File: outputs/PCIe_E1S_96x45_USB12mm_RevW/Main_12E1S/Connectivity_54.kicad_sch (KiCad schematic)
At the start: 12 parts, among them U512 SN74AXC1T45DCKR / HPDA 3.3V t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, U601 9ZXL0851EKILFT / CPU common c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, U602 9ZXL0851EKILFT / CPU common c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, U603 9FGV0241AKLF / DNP ALTERNATE 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, U604 9DML0451AKILF / DNP ALTERNATE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, U605 TPS3808G09DBVR / SUPPORT NETW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, U606 W25Q32JWSSIQ_C2980995 / SUPPO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, U607 TCA9548ARGER / SUPPORT NETWOR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, U701 W25Q256JWPIQ / 1.8V 32MiB BIOS, U702 TPS7A0215PDBVR / RTC 1.5V, U901 TPS548D22RVFR / 0.9004V 40A r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, U902 TPSM63610RDFR / 1.8V 8A

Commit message: Reaudit retained E1S source and improve local converter current paths
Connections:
- net /CPU_PERST_1V8_N renamed /TBT_PCIE_PERST_3V3_N
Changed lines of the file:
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@@
 (kicad_sch (version 20250114) (generator "eeschema") (paper "A2") (title_block (title "Main_12E1S / Connectivity 54") (date "2026-10-17") (rev "W") (comment 1 "FICTIONAL reordered PEX90064 map; CPU288V 32GB MoP; layout and routing study only"))
-(symbol (lib_id "Local:PART_U512") (at 74.93 73.66 0) (unit 1) (in_bom yes) (on_board yes) (dnp no) (property "Reference" "U512" (at 74.93 64.85 0) (effects (font (size 1 1))))(property "Value" "SN74AXC1T45DCKR / HPDA 3.3V to 1.8V" (at 74.93 61.849999999999994 0) (effects (font (size 1 1))))(property "Footprint" "Local:SOT-363_SC-70-6" (at 74.93 73.66 0) (effects (font (size 1 1)) (hide yes)))(pin "1")(pin "2")(pin "3")(pin "4")(pin "5")(pin "6")(instances (project "Main_12E1S" (path "/c33a6c5d-1a9e-4453-a37d-d3058a6ae0e3/4713fd16-f2bf-49a2-84a4-e44d648d003c" (reference "U512") (unit 1)))))
+(symbol (lib_id "Local:PART_U512") (at 74.93 73.66 0) (unit 1) (in_bom yes) (on_board yes) (dnp no) (property "Datasheet" "https://www.ti.com/lit/ds/symlink/sn74axc1t45.pdf" (at 0 0 0) (effects (font (size 1 1)) (hide yes)))(property "Reference" "U512" (at 74.93 64.85 0) (effects (font (size 1 1))))(property "Value" "SN74AXC1T45DCKR / HPDA 3.3V to 1.8V" (at 74.93 61.849999999999994 0) (effects (font (size 1 1))))(property "Footprint" "Local:SOT-363_SC-70-6" (at 74.93 73.66 0) (effects (font (size 1 1)) (hide yes)))(pin "1")(pin "2")(pin "3")(pin "4")(pin "5")(pin "6")(instances (project "Main_12E1S" (path "/c33a6c5d-1a9e-4453-a37d-d3058a6ae0e3/4713fd16-f2bf-49a2-84a4-e44d648d003c" (reference "U512") (unit 1)))))
 (global_label "/CPU_VCCPRIM_1P8" (shape passive) (at 59.690000000000005 71.11999999999999 180) (effects (font (size 0.8 0.8)) (justify right)))
 (global_label "/GND" (shape passive) (at 59.690000000000005 73.66 180) (effects (font (size 0.8 0.8)) (justify right)))
@@
 (global_label "/GND" (shape passive) (at 90.17 212.09 0) (effects (font (size 0.8 0.8)) (justify left)))
 (global_label "/GND" (shape passive) (at 90.17 214.63 0) (effects (font (size 0.8 0.8)) (justify left)))
-(symbol (lib_id "Local:PART_U605") (at 218.44 201.93 0) (unit 1) (in_bom yes) (on_board yes) (dnp no) (property "Reference" "U605" (at 218.44 193.12 0) (effects (font (size 1 1))))(property "Value" "TPS3808G09DBVR / SUPPORT NETWORK PENDING" (at 218.44 190.12 0) (effects (font (size 1 1))))(property "Footprint" "Local:REF_TPS3808G09DBVR_FU1" (at 218.44 201.93 0) (effects (font (size 1 1)) (hide yes)))(pin "1")(pin "2")(pin "3")(pin "4")(pin "5")(pin "6")(instances (project "Main_12E1S" (path "/c33a6c5d-1a9e-4453-a37d-d3058a6ae0e3/4713fd16-f2bf-49a2-84a4-e44d648d003c" (reference "U605") (unit 1)))))
+(symbol (lib_id "Local:PART_U605") (at 218.44 201.93 0) (unit 1) (in_bom yes) (on_board yes) (dnp no) (property "Datasheet" "https://www.ti.com/lit/ds/symlink/tps3808.pdf" (at 0 0 0) (effects (font (size 1 1)) (hide yes)))(property "Reference" "U605" (at 218.44 193.12 0) (effects (font (size 1 1))))(property "Value" "TPS3808G09DBVR / SUPPORT NETWORK PENDING" (at 218.44 190.12 0) (effects (font (size 1 1))))(property "Footprint" "Local:REF_TPS3808G09DBVR_FU1" (at 218.44 201.93 0) (effects (font (size 1 1)) (hide yes)))(pin "1")(pin "2")(pin "3")(pin "4")(pin "5")(pin "6")(instances (project "Main_12E1S" (path "/c33a6c5d-1a9e-4453-a37d-d3058a6ae0e3/4713fd16-f2bf-49a2-84a4-e44d648d003c" (reference "U605") (unit 1)))))
 (global_label "/PEX_SYS_RESET_N" (shape passive) (at 203.2 199.39000000000001 180) (effects (font (size 0.8 0.8)) (justify right)))
 (global_label "/GND" (shape passive) (at 203.2 201.93 180) (effects (font (size 0.8 0.8)) (justify right)))
-(global_label "/CPU_PERST_1V8_N" (shape passive) (at 203.2 204.47 180) (effects (font (size 0.8 0.8)) (justify right)))
+(global_label "/TBT_PCIE_PERST_3V3_N" (shape passive) (at 203.2 204.47 180) (effects (font (size 0.8 0.8)) (justify right)))
 (global_label "/PEX_RESET_CT" (shape passive) (at 233.68 199.39000000000001 0) (effects (font (size 0.8 0.8)) (justify left)))
 (global_label "/PEX_0V9" (shape passive) (at 233.68 201.93 0) (effects (font (size 0.8 0.8)) (justify left)))
@@
 (no_connect (at 233.68 327.65999999999997))
 (global_label "/CPU_VCCRTC" (shape passive) (at 233.68 330.2 0) (effects (font (size 0.8 0.8)) (justify left)))
-(symbol (lib_id "Local:PART_U901") (at 360.68 330.2 0) (unit 1) (in_bom yes) (on_board yes) (dnp no) (property "Reference" "U901" (at 360.68 298.53 0) (effects (font (size 1 1))))(property "Value" "TPS548D22RVFR / 0.9004V 40A reference" (at 360.68 295.53 0) (effects (font (size 1 1))))(property "Footprint" "Local:TI_RVF0040A_TPS548D22" (at 360.68 330.2 0) (effects (font (size 1 1)) (hide yes)))(pin "1")(pin "2")(pin "3")(pin "4")(pin "5")(pin "6")(pin "7")(pin "8")(pin "9")(pin "10")(pin "11")(pin "12")(pin "13")(pin "14")(pin "15")(pin "16")(pin "17")(pin "18")(pin "19")(pin "20")(pin "21")(pin "22")(pin "23")(pin "24")(pin "25")(pin "26")(pin "27")(pin "28")(pin "29")(pin "30")(pin "31")(pin "32")(pin "33")(pin "34")(pin "35")(pin "36")(pin "37")(pin "38")(pin "39")(pin "40")(pin "41")(instances (project "Main_12E1S" (path "/c33a6c5d-1a9e-4453-a37d-d3058a6ae0e3/4713fd16-f2bf-49a2-84a4-e44d648d003c" (reference "U901") (unit 1)))))
+(symbol (lib_id "Local:PART_U901") (at 360.68 330.2 0) (unit 1) (in_bom yes) (on_board yes) (dnp no) (property "Datasheet" "https://www.ti.com/lit/ds/symlink/tps548d22.pdf" (at 0 0 0) (effects (font (size 1 1)) (hide yes)))(property "Reference" "U901" (at 360.68 298.53 0) (effects (font (size 1 1))))(property "Value" "TPS548D22RVFR / 0.9004V 40A reference" (at 360.68 295.53 0) (effects (font (size 1 1))))(property "Footprint" "Local:TI_RVF0040A_TPS548D22" (at 360.68 330.2 0) (effects (font (size 1 1)) (hide yes)))(pin "1")(pin "2")(pin "3")(pin "4")(pin "5")(pin "6")(pin "7")(pin "8")(pin "9")(pin "10")(pin "11")(pin "12")(pin "13")(pin "14")(pin "15")(pin "16")(pin "17")(pin "18")(pin "19")(pin "20")(pin "21")(pin "22")(pin "23")(pin "24")(pin "25")(pin "26")(pin "27")(pin "28")(pin "29")(pin "30")(pin "31")(pin "32")(pin "33")(pin "34")(pin "35")(pin "36")(pin "37")(pin "38")(pin "39")(pin "40")(pin "41")(instances (project "Main_12E1S" (path "/c33a6c5d-1a9e-4453-a37d-d3058a6ae0e3/4713fd16-f2bf-49a2-84a4-e44d648d003c" (reference "U901") (unit 1)))))
 (no_connect (at 345.44 304.8))
 (no_connect (at 345.44 307.34))
@@
 (global_label "/PEX_0V9" (shape passive) (at 375.92 350.52 0) (effects (font (size 0.8 0.8)) (justify left)))
 (global_label "/GND" (shape passive) (at 375.92 353.06 0) (effects (font (size 0.8 0.8)) (justify left)))
-(symbol (lib_id "Local:PART_U902") (at 504.19 330.2 0) (unit 1) (in_bom yes) (on_board yes) (dnp no) (property "Reference" "U902" (at 504.19 311.22999999999996 0) (effects (font (size 1 1))))(property "Value" "TPSM63610RDFR / 1.8V 8A" (at 504.19 308.22999999999996 0) (effects (font (size 1 1))))(property "Footprint" "Local:TI_RDF0022A_TPSM63610_NotchedLand" (at 504.19 330.2 0) (effects (font (size 1 1)) (hide yes)))(pin "1")(pin "2")(pin "3")(pin "4")(pin "5")(pin "6")(pin "7")(pin "8")(pin "9")(pin "10")(pin "11")(pin "12")(pin "13")(pin "14")(pin "15")(pin "16")(pin "17")(pin "18")(pin "19")(pin "20")(pin "21")(pin "22")(instances (project "Main_12E1S" (path "/c33a6c5d-1a9e-4453-a37d-d3058a6ae0e3/4713fd16-f2bf-49a2-84a4-e44d648d003c" (reference "U902") (unit 1)))))
+(symbol (lib_id "Local:PART_U902") (at 504.19 330.2 0) (unit 1) (in_bom yes) (on_board yes) (dnp no) (property "Datasheet" "https://www.ti.com/lit/ds/symlink/tpsm63610.pdf" (at 0 0 0) (effects (font (size 1 1)) (hide yes)))(property "Reference" "U902" (at 504.19 311.22999999999996 0) (effects (font (size 1 1))))(property "Value" "TPSM63610RDFR / 1.8V 8A" (at 504.19 308.22999999999996 0) (effects (font (size 1 1))))(property "Footprint" "Local:TI_RDF0022A_TPSM63610_NotchedLand" (at 504.19 330.2 0) (effects (font (size 1 1)) (hide yes)))(pin "1")(pin "2")(pin "3")(pin "4")(pin "5")(pin "6")(pin "7")(pin "8")(pin "9")(pin "10")(pin "11")(pin "12")(pin "13")(pin "14")(pin "15")(pin "16")(pin "17")(pin "18")(pin "19")(pin "20")(pin "21")(pin "22")(instances (project "Main_12E1S" (path "/c33a6c5d-1a9e-4453-a37d-d3058a6ae0e3/4713fd16-f2bf-49a2-84a4-e44d648d003c" (reference "U902") (unit 1)))))
 (global_label "/VBANK_B" (shape passive) (at 488.95 317.5 180) (effects (font (size 0.8 0.8)) (justify right)))
 (global_label "/PEX18_RBOOT" (shape passive) (at 488.95 320.03999999999996 180) (effects (font (size 0.8 0.8)) (justify right)))

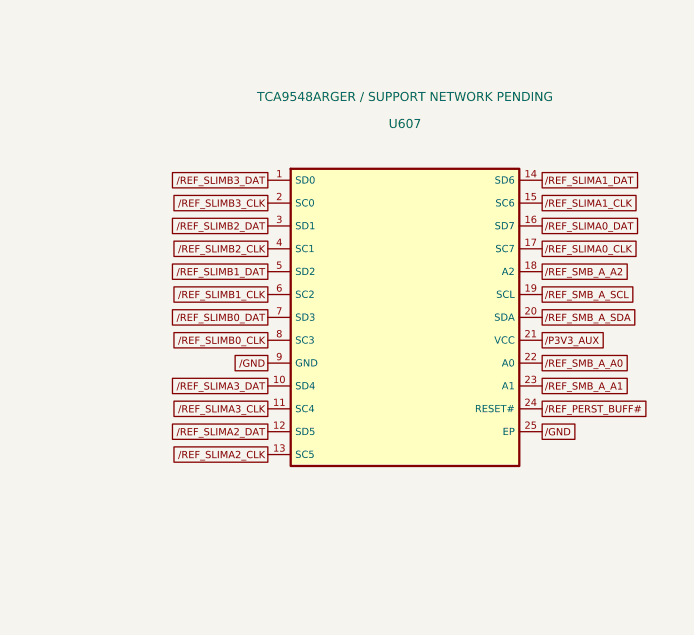
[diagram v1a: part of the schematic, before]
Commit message: Correct E1S BP bypass and support devices; rebuild one PCIe pair
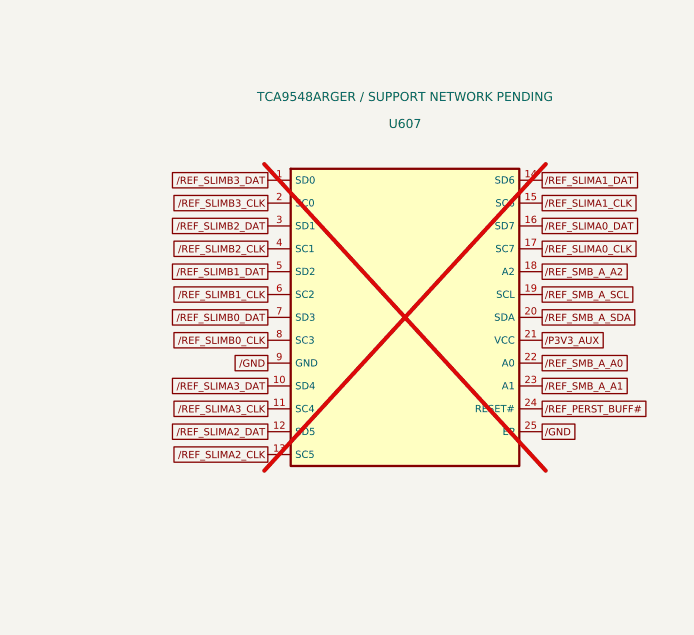
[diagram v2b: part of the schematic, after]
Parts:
- U607: now not fitted
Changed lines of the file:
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@@
 (global_label "/PEX_SPI_IO3" (shape passive) (at 375.92 203.20000000000002 0) (effects (font (size 0.8 0.8)) (justify left)))
 (global_label "/PEX_1V8" (shape passive) (at 375.92 205.74 0) (effects (font (size 0.8 0.8)) (justify left)))
-(symbol (lib_id "Local:PART_U607") (at 504.19 201.93 0) (unit 1) (in_bom yes) (on_board yes) (dnp no) (property "Reference" "U607" (at 504.19 180.42000000000002 0) (effects (font (size 1 1))))(property "Value" "TCA9548ARGER / SUPPORT NETWORK PENDING" (at 504.19 177.42000000000002 0) (effects (font (size 1 1))))(property "Footprint" "Local:REF_TCA9548ARGER_SU1" (at 504.19 201.93 0) (effects (font (size 1 1)) (hide yes)))(pin "1")(pin "2")(pin "3")(pin "4")(pin "5")(pin "6")(pin "7")(pin "8")(pin "9")(pin "10")(pin "11")(pin "12")(pin "13")(pin "14")(pin "15")(pin "16")(pin "17")(pin "18")(pin "19")(pin "20")(pin "21")(pin "22")(pin "23")(pin "24")(pin "25")(instances (project "Main_12E1S" (path "/c33a6c5d-1a9e-4453-a37d-d3058a6ae0e3/4713fd16-f2bf-49a2-84a4-e44d648d003c" (reference "U607") (unit 1)))))
+(symbol (lib_id "Local:PART_U607") (at 504.19 201.93 0) (unit 1) (in_bom yes) (on_board yes) (dnp yes) (property "Reference" "U607" (at 504.19 180.42000000000002 0) (effects (font (size 1 1))))(property "Value" "TCA9548ARGER / SUPPORT NETWORK PENDING" (at 504.19 177.42000000000002 0) (effects (font (size 1 1))))(property "Footprint" "Local:REF_TCA9548ARGER_SU1" (at 504.19 201.93 0) (effects (font (size 1 1)) (hide yes)))(pin "1")(pin "2")(pin "3")(pin "4")(pin "5")(pin "6")(pin "7")(pin "8")(pin "9")(pin "10")(pin "11")(pin "12")(pin "13")(pin "14")(pin "15")(pin "16")(pin "17")(pin "18")(pin "19")(pin "20")(pin "21")(pin "22")(pin "23")(pin "24")(pin "25")(instances (project "Main_12E1S" (path "/c33a6c5d-1a9e-4453-a37d-d3058a6ae0e3/4713fd16-f2bf-49a2-84a4-e44d648d003c" (reference "U607") (unit 1)))))
 (global_label "/REF_SLIMB3_DAT" (shape passive) (at 488.95 186.69 180) (effects (font (size 0.8 0.8)) (justify right)))
 (global_label "/REF_SLIMB3_CLK" (shape passive) (at 488.95 189.23000000000002 180) (effects (font (size 0.8 0.8)) (justify right)))
